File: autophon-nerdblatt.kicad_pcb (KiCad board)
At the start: 2 copper layers, 265 x 140 mm, 18 parts, among them J1 board-edge-connector, U1 74HC74, U2 L298HN, U3 L298HN, U4 L298HN, U5 74AHC04, U6 74HC74, U7 74HC74

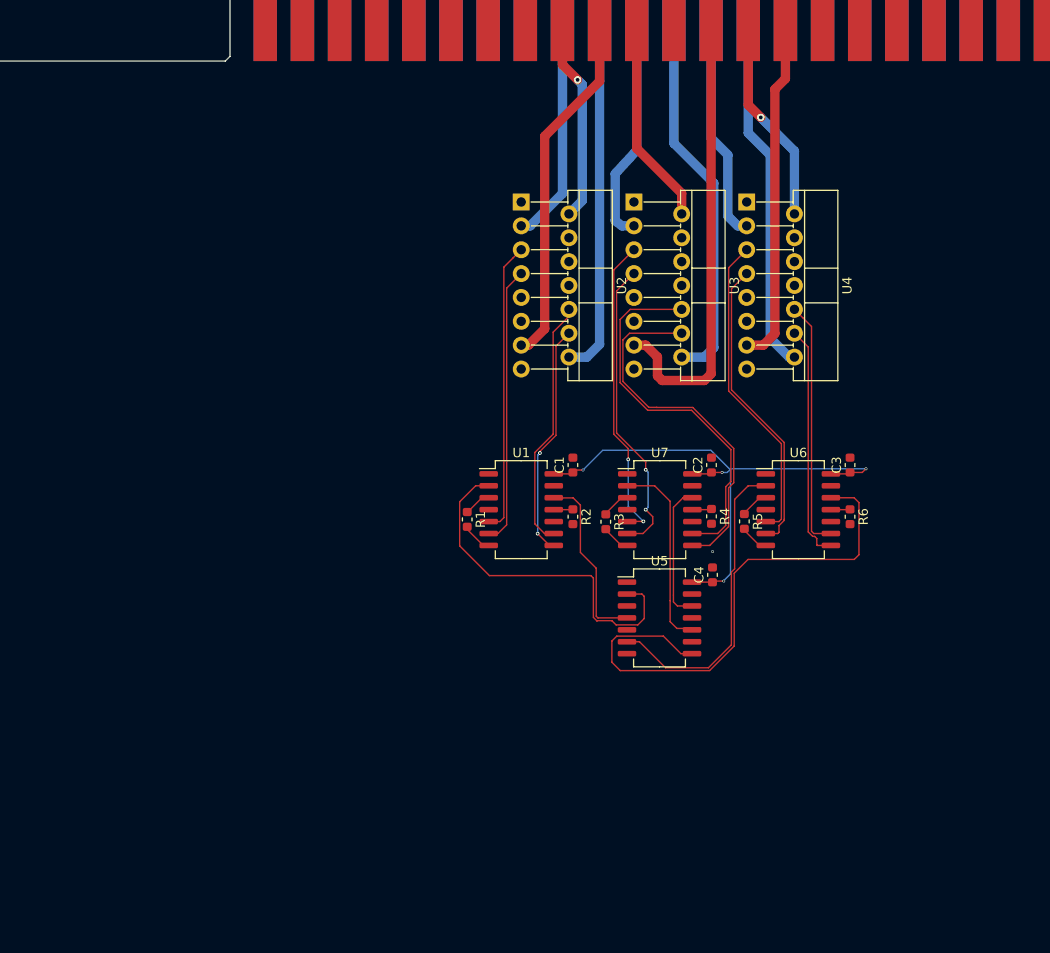
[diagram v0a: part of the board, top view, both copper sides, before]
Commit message: Added footprints.
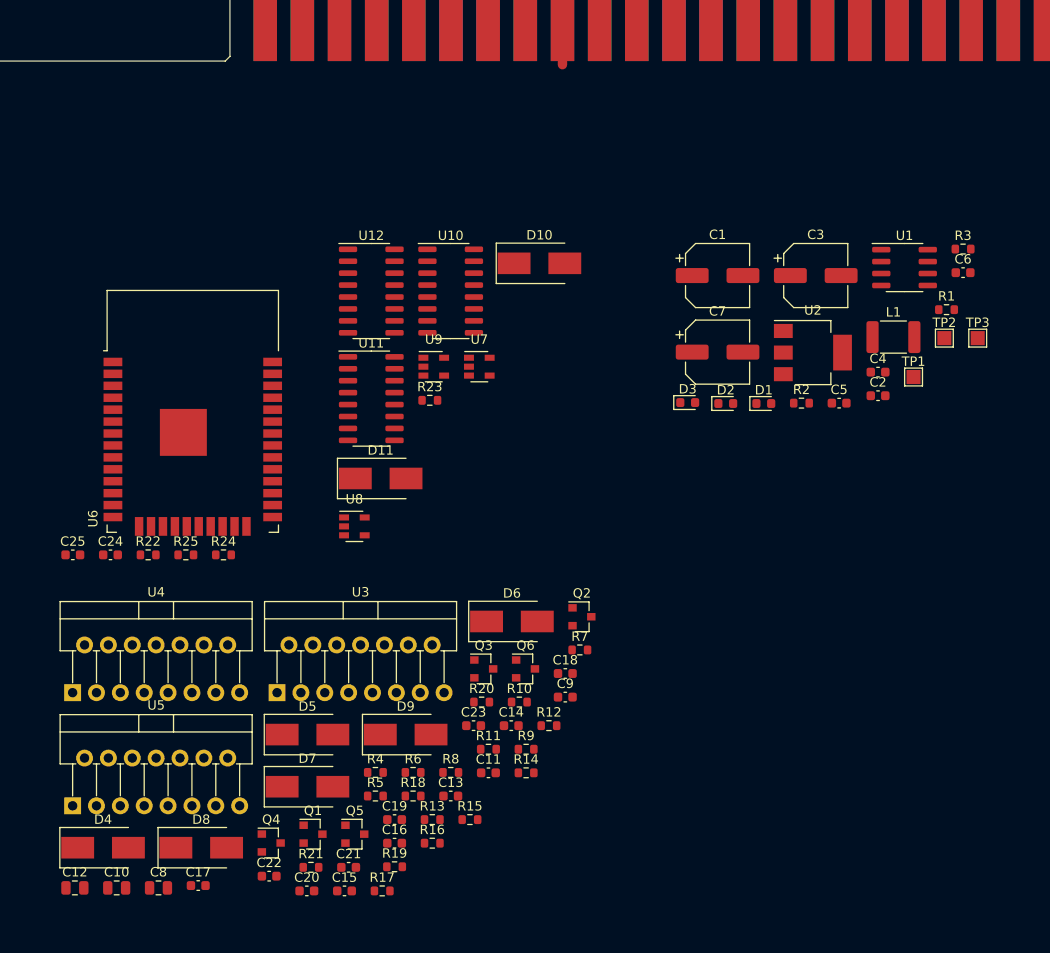
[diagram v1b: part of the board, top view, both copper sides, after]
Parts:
- added C10: 10u, Capacitor_SMD:C_0805_2012Metric, F.Cu at (215.4, 165.5)
- added C11: 100n, Capacitor_SMD:C_0603_1608Metric, F.Cu at (255.0, 153.3)
- added C12: 10u, Capacitor_SMD:C_0805_2012Metric, F.Cu at (211.0, 165.5)
- added C13: 100n, Capacitor_SMD:C_0603_1608Metric, F.Cu at (251.0, 155.7)
- added C14: 100n, Capacitor_SMD:C_0603_1608Metric, F.Cu at (257.4, 148.2)
- added C15: 100n, Capacitor_SMD:C_0603_1608Metric, F.Cu at (239.7, 165.8)
- added C16: 100n, Capacitor_SMD:C_0603_1608Metric, F.Cu at (245.0, 160.8)
- added C17: 100n, Capacitor_SMD:C_0603_1608Metric, F.Cu at (224.1, 165.3)
- added C18: 100n, Capacitor_SMD:C_0603_1608Metric, F.Cu at (263.2, 142.7)
- added C19: 100n, Capacitor_SMD:C_0603_1608Metric, F.Cu at (245.0, 158.2)
- added C20: 100n, Capacitor_SMD:C_0603_1608Metric, F.Cu at (235.7, 165.8)
- added C21: 100n, Capacitor_SMD:C_0603_1608Metric, F.Cu at (240.1, 163.3)
- added C22: 100n, Capacitor_SMD:C_0603_1608Metric, F.Cu at (231.7, 164.3)
- added C23: 100n, Capacitor_SMD:C_0603_1608Metric, F.Cu at (253.4, 148.2)
- added C24: C, Capacitor_SMD:C_0603_1608Metric, F.Cu at (214.8, 130.1)
- added C25: C, Capacitor_SMD:C_0603_1608Metric, F.Cu at (210.8, 130.1)
- added C5: 100n, Capacitor_SMD:C_0603_1608Metric, F.Cu at (292.3, 113.9)
- added C6: 100n, Capacitor_SMD:C_0603_1608Metric, F.Cu at (305.5, 100.0)
- added C7: 22u, Capacitor_SMD:CP_Elec_6.3x7.7, F.Cu at (279.4, 108.5)
- added C8: 10u, Capacitor_SMD:C_0805_2012Metric, F.Cu at (219.9, 165.5)
- added C9: 100n, Capacitor_SMD:C_0603_1608Metric, F.Cu at (263.2, 145.2)
- added D1: LED, LED_SMD:LED_0603_1608Metric, F.Cu at (284.3, 114.0)
- added D10: 5v1, Diode_SMD:D_SMB_Handsoldering, F.Cu at (260.4, 99.0)
- added D11: 5v1, Diode_SMD:D_SMB_Handsoldering, F.Cu at (243.5, 121.9)
- added D2: LED, LED_SMD:LED_0603_1608Metric, F.Cu at (280.3, 114.0)
- added D3: LED, LED_SMD:LED_0603_1608Metric, F.Cu at (276.2, 113.8)
- added D4: 5v1, Diode_SMD:D_SMB_Handsoldering, F.Cu at (214.0, 161.2)
- added D5: 5v1, Diode_SMD:D_SMB_Handsoldering, F.Cu at (235.8, 149.2)
- added D6: 5v1, Diode_SMD:D_SMB_Handsoldering, F.Cu at (257.5, 137.2)
- added D7: 5v1, Diode_SMD:D_SMB_Handsoldering, F.Cu at (235.8, 154.7)
- added D8: 5v1, Diode_SMD:D_SMB_Handsoldering, F.Cu at (224.4, 161.2)
- added D9: 5v1, Diode_SMD:D_SMB_Handsoldering, F.Cu at (246.2, 149.2)
- added L1: 100u, Inductor_SMD:L_1812_4532Metric_Pad1.30x3.40mm_HandSolder, F.Cu at (298.1, 106.9)
- added Q1: BSS84, Package_TO_SOT_SMD:SOT-23, F.Cu at (236.3, 159.8)
- added Q2: BSS84, Package_TO_SOT_SMD:SOT-23, F.Cu at (265.0, 136.7)
- added Q3: BSS84, Package_TO_SOT_SMD:SOT-23, F.Cu at (254.5, 142.2)
- added Q4: BSS84, Package_TO_SOT_SMD:SOT-23, F.Cu at (231.9, 160.7)
- added Q5: BSS84, Package_TO_SOT_SMD:SOT-23, F.Cu at (240.8, 159.8)
- added Q6: BSS84, Package_TO_SOT_SMD:SOT-23, F.Cu at (259.0, 142.2)
- added R10: 10k, Resistor_SMD:R_0603_1608Metric, F.Cu at (258.3, 145.7)
- added R11: 10k, Resistor_SMD:R_0603_1608Metric, F.Cu at (255.0, 150.8)
- added R12: 10k, Resistor_SMD:R_0603_1608Metric, F.Cu at (261.4, 148.2)
- added R13: 10k, Resistor_SMD:R_0603_1608Metric, F.Cu at (249.0, 158.2)
- added R14: 10k, Resistor_SMD:R_0603_1608Metric, F.Cu at (259.0, 153.3)
- added R15: 10k, Resistor_SMD:R_0603_1608Metric, F.Cu at (253.0, 158.2)
- added R16: 51R, Resistor_SMD:R_0603_1608Metric, F.Cu at (249.0, 160.8)
- added R17: 51R, Resistor_SMD:R_0603_1608Metric, F.Cu at (243.7, 165.8)
- added R18: 51R, Resistor_SMD:R_0603_1608Metric, F.Cu at (247.0, 155.7)
- added R19: 51R, Resistor_SMD:R_0603_1608Metric, F.Cu at (245.0, 163.3)
- added R20: 51R, Resistor_SMD:R_0603_1608Metric, F.Cu at (254.3, 145.7)
- added R21: 51R, Resistor_SMD:R_0603_1608Metric, F.Cu at (236.1, 163.3)
- added R22: R, Resistor_SMD:R_0603_1608Metric, F.Cu at (218.8, 130.1)
- added R23: R, Resistor_SMD:R_0603_1608Metric, F.Cu at (248.8, 113.6)
- added R24: R, Resistor_SMD:R_0603_1608Metric, F.Cu at (226.8, 130.1)
- added R25: 10k, Resistor_SMD:R_0603_1608Metric, F.Cu at (222.8, 130.1)
- added R7: 10k, Resistor_SMD:R_0603_1608Metric, F.Cu at (264.7, 140.2)
- added R8: 10k, Resistor_SMD:R_0603_1608Metric, F.Cu at (251.0, 153.2)
- added R9: 10k, Resistor_SMD:R_0603_1608Metric, F.Cu at (259.0, 150.8)
- added TP1: 24V, TestPoint:TestPoint_Pad_1.5x1.5mm, F.Cu at (300.3, 111.1)
- added TP2: 5V, TestPoint:TestPoint_Pad_1.5x1.5mm, F.Cu at (303.5, 107.0)
- added TP3: VCC, TestPoint:TestPoint_Pad_1.5x1.5mm, F.Cu at (307.1, 107.0)
- added U10: 74AHCT595, Package_SO:SOIC-16_3.9x9.9mm_P1.27mm, F.Cu at (251.0, 102.0)
- added U11: 74AHCT595, Package_SO:SOIC-16_3.9x9.9mm_P1.27mm, F.Cu at (242.5, 113.4)
- added U12: 74AHCT595, Package_SO:SOIC-16_3.9x9.9mm_P1.27mm, F.Cu at (242.5, 102.0)
- added U8: SN74LV1T34, Package_TO_SOT_SMD:SOT-23-5, F.Cu at (240.7, 127.0)
- added U9: SN74LV1T34, Package_TO_SOT_SMD:SOT-23-5, F.Cu at (249.2, 110.0)
- C1: value C -> 120u; footprint Capacitor_SMD:C_0603_1608Metric -> Capacitor_SMD:CP_Elec_6.3x7.7
- C2, C4: value C -> 100n
- C3: value C -> 39u; footprint Capacitor_SMD:C_0603_1608Metric -> Capacitor_SMD:CP_Elec_6.3x7.7
- R1, R2, R3, R4, R5, R6: value R -> 10k
- U1: value 74HC74 -> LM2594M-5.0; footprint Package_SO:SO-14_5.3x10.2mm_P1.27mm -> Package_SO:SOIC-8_3.9x4.9mm_P1.27mm
- U2: value L298HN -> AZ1117-3.3; footprint Package_TO_SOT_THT:TO-220F-15_P2.54x5.08mm_StaggerOdd_Lead5.08mm_Vertical -> Package_TO_SOT_SMD:SOT-223-3_TabPin2
- U3, U4: footprint Package_TO_SOT_THT:TO-220F-15_P2.54x5.08mm_StaggerOdd_Lead5.08mm_Vertical -> Package_TO_SOT_THT:TO-220-15_P2.54x2.54mm_StaggerOdd_Lead4.58mm_Vertical
- U5: value 74AHC04 -> L298HN; footprint Package_SO:SO-14_5.3x10.2mm_P1.27mm -> Package_TO_SOT_THT:TO-220-15_P2.54x2.54mm_StaggerOdd_Lead4.58mm_Vertical
- U6: value 74HC74 -> ESP32-WROOM-32; footprint Package_SO:SO-14_5.3x10.2mm_P1.27mm -> RF_Module:ESP32-WROOM-32
- U7: value 74HC74 -> SN74LV1T34; footprint Package_SO:SO-14_5.3x10.2mm_P1.27mm -> Package_TO_SOT_SMD:SOT-23-5
- moved U4 88.7 mm to (210.8, 144.7), turned to 0 degrees
- moved U5 65.6 mm to (210.8, 156.8)
- moved U6 64.9 mm to (223.5, 117.8)
- moved U3 64.6 mm to (232.5, 144.7), turned to 0 degrees
- moved R1 55.7 mm to (303.8, 104.0), turned to 0 degrees
- moved R6 53.9 mm to (247.0, 153.2), turned to 0 degrees
- moved R5 49.0 mm to (243.0, 155.7), turned to 0 degrees
- moved U1 48.3 mm to (299.3, 99.5)
- moved R3 47.8 mm to (305.5, 97.5), turned to 0 degrees
- moved R4 45.0 mm to (243.0, 153.2), turned to 0 degrees
- moved U2 34.9 mm to (289.6, 108.5), turned to 0 degrees
- moved C4 27.9 mm to (296.5, 110.6), turned to 0 degrees
- moved R2 27.2 mm to (288.3, 113.9), turned to 0 degrees
- moved C1 25.4 mm to (279.4, 100.3), turned to 0 degrees
- moved U7 24.5 mm to (254.0, 110.0)
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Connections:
- net ABCDEF.5 renamed ABCDEF_HALL_GND
- net Net-(U5-Pad13) renamed F_MOT_POS
- net Net-(U5-Pad5) renamed E_MOT_POS_DRV
- C1 pad 1: +5V -> +24V
- C2 pad 1: +5V -> +24V
- J1 pad 10B: E.2 -> E_MOT_NEG
- J1 pad 11B: D.2 -> D_MOT_NEG
- J1 pad 12B: C.2 -> C_MOT_NEG
- J1 pad 13B: B.2 -> B_MOT_NEG
- J1 pad 14B: A.2 -> A_MOT_NEG
- J1 pad 19B: ABCDEF.6 -> ABCDEF_HALL_ROTOR
- J1 pad 20B: ABCDEF.4 -> ABCDEF_HALL_INDEX
- J1 pad 23A: A.3 -> A_HALL_PWR
- J1 pad 24A: B.3 -> B_HALL_PWR
- J1 pad 25A: C.3 -> C_HALL_PWR
- J1 pad 27A: D.3 -> D_HALL_PWR
- J1 pad 28A: E.3 -> E_HALL_PWR
- J1 pad 29A: F.3 -> F_HALL_PWR
- J1 pad 31A: A.1 -> A_MOT_POS
- J1 pad 32A: B.1 -> B_MOT_POS
- J1 pad 33A: C.1 -> C_MOT_POS
- J1 pad 35A: D.1 -> D_MOT_POS
- J1 pad 36A: E.1 -> E_MOT_POS
- J1 pad 37A: F.1 -> F_MO_POS
- J1 pad 9B: F.2 -> F_MOT_NEG
- R1 pad 1: Net-(R1-Pad1) -> +24V
- R1 pad 2: GND -> Net-(D1-Pad2)
- R2 pad 1: Net-(R2-Pad1) -> +5V
- R2 pad 2: GND -> Net-(D2-Pad2)
- R3 pad 1: Net-(R3-Pad1) -> VCC
- R3 pad 2: GND -> Net-(D3-Pad2)
- R4 pad 1: Net-(R4-Pad1) -> +5V
- R4 pad 2: GND -> ~A_HALL_PWR_EN~
- R5 pad 1: Net-(R5-Pad1) -> +5V
- R5 pad 2: GND -> ~B_HALL_PWR_EN~
- R6 pad 1: Net-(R6-Pad1) -> +5V
- R6 pad 2: GND -> ~C_HALL_PWR_EN~
- U1 pad 3: Net-(R1-Pad1) -> Net-(U1-Pad3)
- U1 pad 4: Net-(U1-Pad4) -> +5V
- U1 pad 5: A_IN1 -> Net-(U1-Pad5)
- U1 pad 6: A_IN2 -> GND
- U1 pad 7: GND -> +24V
- U1 pad 8: B_IN4 -> Net-(L1-Pad1)
- U2 pad 2: A.1 -> VCC
- U2 pad 3: A.2 -> +5V
- U3 pad 1: Net-(U3-Pad1) -> GND
- U3 pad 10: D_IN3 -> B_MOT_POS_DRV
- U3 pad 11: D_EN -> GLOBAL_MOT_EN
- U3 pad 12: D_IN4 -> B_MOT_NEG_DRV
- U3 pad 13: D.1 -> B_MOT_POS
- U3 pad 14: D.2 -> B_MOT_NEG
- U3 pad 15: Net-(U3-Pad15) -> GND
- U3 pad 2: C.1 -> A_MOT_POS
- U3 pad 3: C.2 -> A_MOT_NEG
- U3 pad 4: Net-(U3-Pad4) -> +5V
- U3 pad 5: C_IN1 -> A_MOT_POS_DRV
- U3 pad 6: C_EN -> GLOBAL_MOT_EN
- U3 pad 7: C_IN2 -> A_MOT_NEG_DRV
- U3 pad 9: Net-(U3-Pad9) -> +24V
- U4 pad 1: Net-(U4-Pad1) -> GND
- U4 pad 10: F_IN3 -> D_MOT_POS_DRV
- U4 pad 11: F_EN -> GLOBAL_MOT_EN
- U4 pad 12: F_IN4 -> D_MOT_NEG_DRV
- U4 pad 13: F.1 -> D_MOT_POS
- U4 pad 14: F.2 -> D_MOT_NEG
- U4 pad 15: Net-(U4-Pad15) -> GND
- U4 pad 2: E.1 -> C_MOT_POS
- U4 pad 3: E.2 -> C_MOT_NEG
- U4 pad 4: Net-(U4-Pad4) -> +5V
- U4 pad 5: E_IN1 -> C_MOT_POS_DRV
- U4 pad 6: E_EN -> GLOBAL_MOT_EN
- U4 pad 7: E_IN2 -> C_MOT_NEG_DRV
- U4 pad 9: Net-(U4-Pad9) -> +24V
- U5 pad 1: Net-(U5-Pad1) -> GND
- U5 pad 10: Net-(U5-Pad10) -> F_MOT_POS_DRV
- U5 pad 11: Net-(U5-Pad11) -> GLOBAL_MOT_EN
- U5 pad 12: Net-(U5-Pad12) -> F_MOT_NEG_DRV
- U5 pad 14: +5V -> F_MOT_NEG
- U5 pad 2: Net-(U1-Pad2) -> E_MOT_POS
- U5 pad 3: Net-(U5-Pad3) -> E_MOT_NEG
- U5 pad 4: Net-(U1-Pad12) -> +5V
- U5 pad 6: Net-(U5-Pad6) -> GLOBAL_MOT_EN
- U5 pad 7: GND -> E_MOT_NEG_DRV
- U5 pad 8: Net-(U5-Pad8) -> GND
- U5 pad 9: Net-(U5-Pad9) -> +24V
- U6 pad 10: Net-(U6-Pad10) -> /ESP32_Shiftregs/~HALL_EN_3V~
- U6 pad 11: Net-(R6-Pad1) -> /ESP32_Shiftregs/MOT_EN_3V
- U6 pad 12: Net-(U5-Pad8) -> /ESP32_Shiftregs/HALL_ROTOR_3V
- U6 pad 14: +5V -> Net-(U6-Pad14)
- U6 pad 2: Net-(U5-Pad6) -> Net-(U6-Pad2)
- U6 pad 3: Net-(R5-Pad1) -> Net-(U6-Pad3)
- U6 pad 5: E_IN1 -> Net-(U6-Pad5)
- U6 pad 6: E_IN2 -> /ESP32_Shiftregs/SPI_SCLK
- U6 pad 7: GND -> /ESP32_Shiftregs/~SPI_CS0~
- U6 pad 8: F_IN4 -> /ESP32_Shiftregs/HALL_INDEX_3V
- U6 pad 9: F_IN3 -> /ESP32_Shiftregs/SPI_COPI
- U7 pad 1: Net-(U7-Pad1) -> (no net)
- U7 pad 2: Net-(U5-Pad10) -> ABCDEF_HALL_ROTOR
- U7 pad 3: Net-(R3-Pad1) -> GND
- U7 pad 4: Net-(U7-Pad4) -> /ESP32_Shiftregs/HALL_ROTOR_3V
- U7 pad 5: C_IN1 -> VCC
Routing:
- net +5V: track 59.0 -> 0.00 mm, vias 4 -> 0
- net Net-(U5-Pad8): track 57.8 -> 0.00 mm
- net D.1: track 44.5 -> 0.00 mm
- net D_IN3: track 40.7 -> 0.00 mm
- net D_IN4: track 39.0 -> 0.00 mm
- net Net-(U1-Pad2): track 38.6 -> 0.00 mm
- net D.2: track 36.1 -> 0.00 mm
- net B.1: track 34.1 -> 0.00 mm
- net B.2: track 34.0 -> 0.00 mm
- net F.2: track 33.9 -> 0.00 mm
- net E_IN1: track 33.6 -> 0.00 mm
- net F.1: track 33.0 -> 0.00 mm
- net C_IN1: track 32.8 -> 0.00 mm, vias 2 -> 0
- net Net-(U5-Pad6): track 32.8 -> 0.00 mm
- net C_IN2: track 32.3 -> 0.00 mm, vias 2 -> 0
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
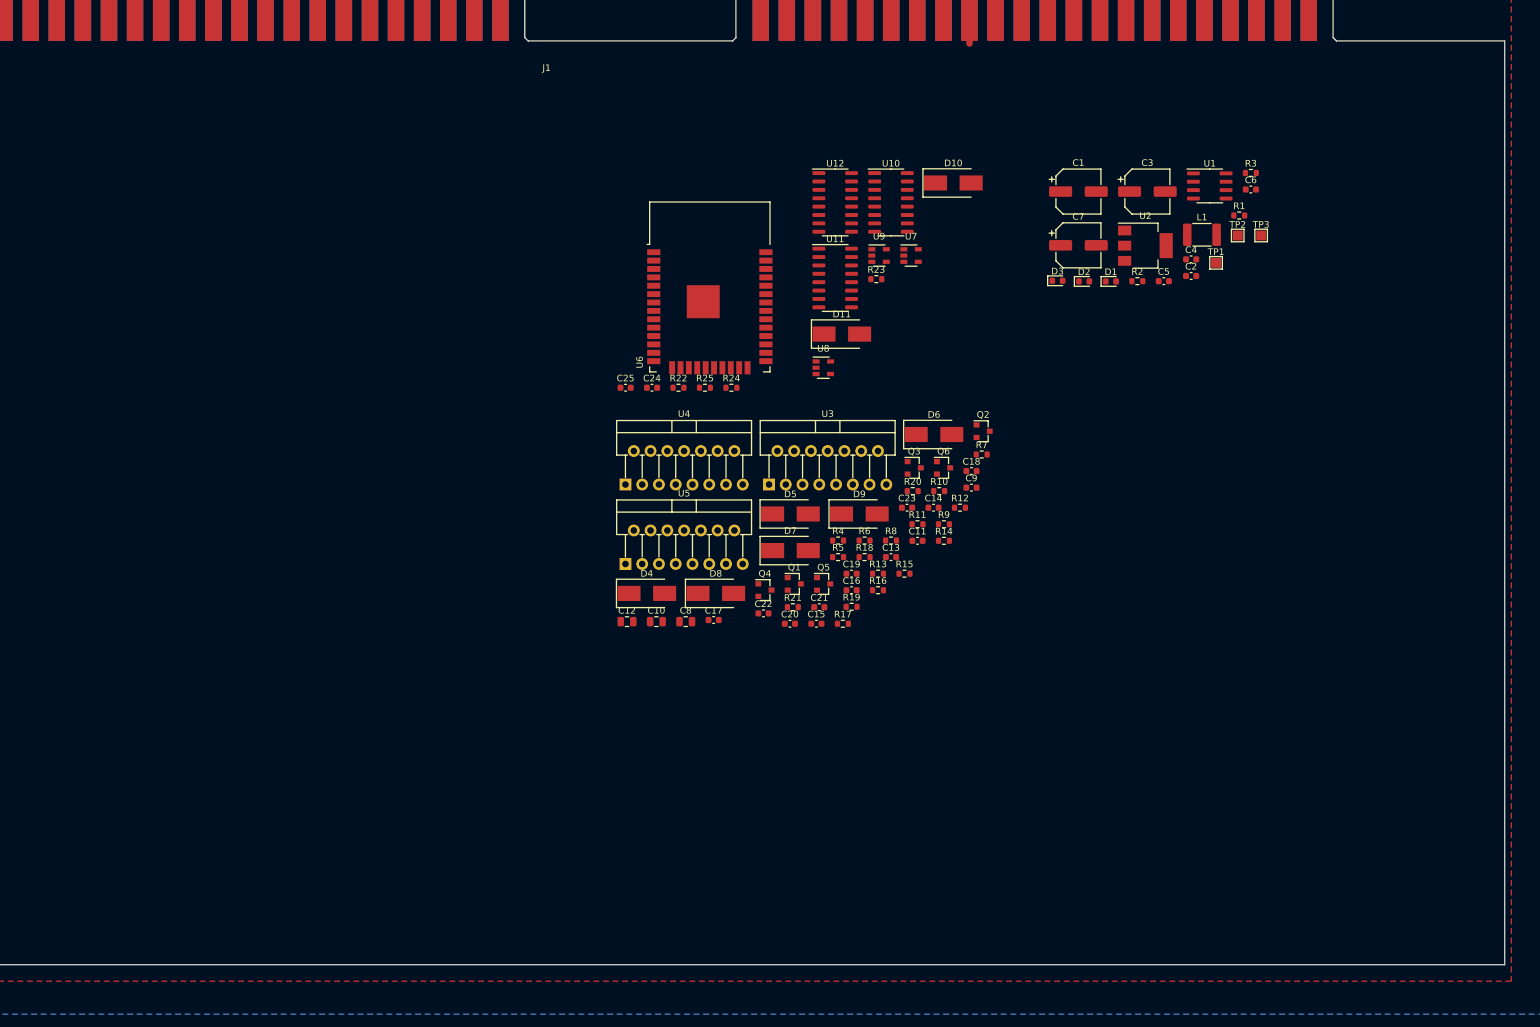
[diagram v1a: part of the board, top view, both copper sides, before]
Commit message: caps for long high impedance traces. distributor info.
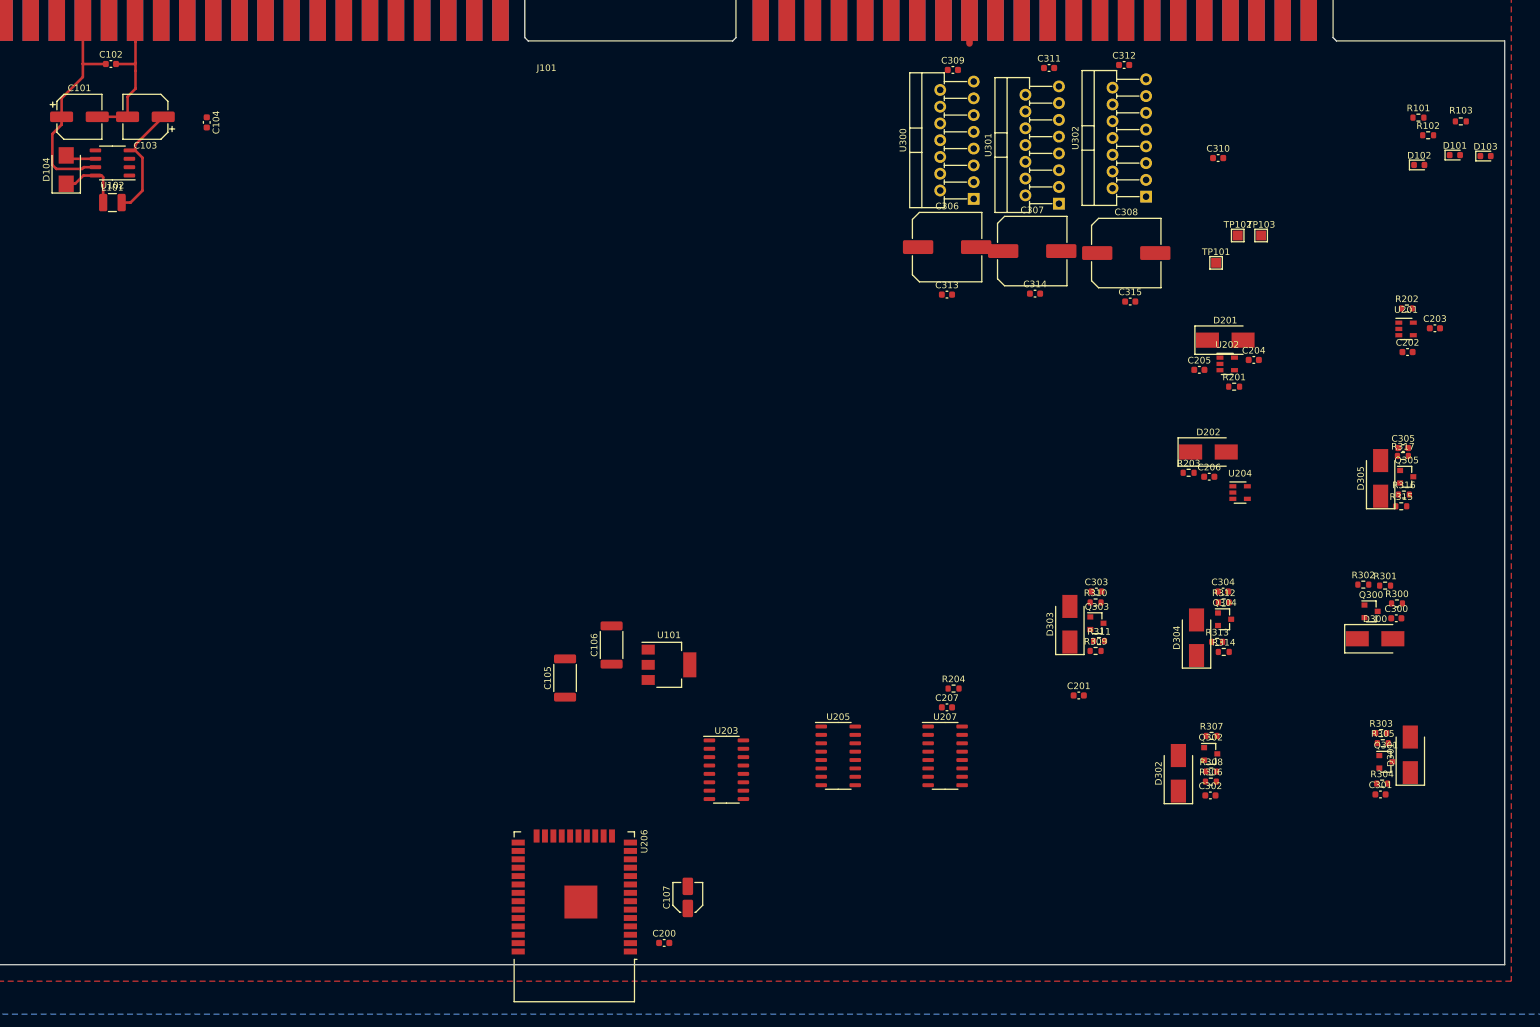
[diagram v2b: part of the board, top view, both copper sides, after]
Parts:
- removed C10, C12, C8: 10u, Capacitor_SMD:C_0805_2012Metric
- removed C5, C6: 100n, Capacitor_SMD:C_0603_1608Metric
- removed U2: AZ1117-3.3, Package_TO_SOT_SMD:SOT-223-3_TabPin2
- added C105: 10u, Capacitor_SMD:C_2512_6332Metric, F.Cu at (201.6, 174.1)
- added C106: 10u, Capacitor_SMD:C_2512_6332Metric, F.Cu at (208.7, 169.1)
- added C200: 100n, Capacitor_SMD:C_0603_1608Metric, F.Cu at (216.6, 214.2)
- added C201: 100n, Capacitor_SMD:C_0603_1608Metric, F.Cu at (279.4, 176.7)
- added C202: 1n, Capacitor_SMD:C_0603_1608Metric, F.Cu at (329.3, 124.7)
- added C204: 1n, Capacitor_SMD:C_0603_1608Metric, F.Cu at (306.0, 125.8)
- added C206: 1n, Capacitor_SMD:C_0603_1608Metric, F.Cu at (299.2, 143.6)
- added C207: 1n, Capacitor_SMD:C_0603_1608Metric, F.Cu at (259.5, 178.5)
- added C306: 470uF, Capacitor_SMD:C_Elec_10x10.2, F.Cu at (259.5, 108.8)
- added C307: 470uF, Capacitor_SMD:C_Elec_10x10.2, F.Cu at (272.4, 109.3)
- added C308: 470uF, Capacitor_SMD:C_Elec_10x10.2, F.Cu at (286.6, 109.7)
- added D104: MBRS130, Diode_SMD:D_SMB, F.Cu at (126.0, 97.0)
- added U101: LM1117-3.3, Package_TO_SOT_SMD:SOT-223-3_TabPin2, F.Cu at (217.3, 172.1)
- C102: renamed from C2; value 100n -> 100n/25V
- C103: renamed from C3; value 39u -> 120u
- C107: renamed from C7; footprint Capacitor_SMD:CP_Elec_6.3x7.7 -> Capacitor_SMD:C_Elec_4x5.8
- C203: renamed from C25; value C -> 1n
- C205: renamed from C24; value C -> 1n
- C313: renamed from C9; value 100n -> 100n/25V
- C314: renamed from C11; value 100n -> 100n/25V
- C315: renamed from C13; value 100n -> 100n/25V
- D101: renamed from D1; value LED -> LED gn
- D102: renamed from D2; value LED -> LED gn
- D103: renamed from D3; value LED -> LED gn
- L101: renamed from L1; value 100u -> 100uH; footprint Inductor_SMD:L_1812_4532Metric_Pad1.30x3.40mm_HandSolder -> Inductor_SMD:L_1210_3225Metric
- R101: renamed from R1; value 10k -> 1k2
- R102: renamed from R2; value 10k -> 200R
- R103: renamed from R3; value 10k -> 100R
- R201: renamed from R23; value R -> 4k7
- R203: renamed from R22; value R -> 4k7
- R204: renamed from R24; value R -> 10k
- U102: renamed from U1; footprint Package_SO:SOIC-8_3.9x4.9mm_P1.27mm -> Package_SO:SO-8_3.9x4.9mm_P1.27mm
- U203: renamed from U10; footprint Package_SO:SOIC-16_3.9x9.9mm_P1.27mm -> Package_SO:SO-16_3.9x9.9mm_P1.27mm
- U205: renamed from U11; footprint Package_SO:SOIC-16_3.9x9.9mm_P1.27mm -> Package_SO:SO-16_3.9x9.9mm_P1.27mm
- U207: renamed from U12; footprint Package_SO:SOIC-16_3.9x9.9mm_P1.27mm -> Package_SO:SO-16_3.9x9.9mm_P1.27mm
- moved C102 166.8 mm to (132.8, 81.0)
- moved U102 166.3 mm to (133.0, 96.0), turned to 180 degrees
- moved L101 165.2 mm to (133.0, 102.0)
- moved C103 152.3 mm to (138.0, 89.0), turned to 180 degrees
- moved C101 151.8 mm to (128.0, 89.0)
- moved C104 150.6 mm to (147.3, 89.8), turned to -90 degrees
- moved C203 123.0 mm to (333.4, 121.0)
- moved C107 115.2 mm to (220.2, 207.3), turned to 90 degrees
- moved D300 110.6 mm to (324.4, 168.1)
- moved R202 107.1 mm to (329.2, 118.0)
- moved C312 104.6 mm to (286.3, 81.2)
- moved D301 100.8 mm to (329.7, 185.7), turned to 90 degrees
- moved U302 96.6 mm to (289.6, 101.1), turned to 90 degrees
- moved R315 93.5 mm to (328.3, 148.0)
- moved C310 93.2 mm to (300.6, 95.2)
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- renumbered C1 to C101, C4 to C104, C18 to C300, C19 to C301, C20 to C302, C21 to C303, C22 to C304, C23 to C305, C14 to C309, C15 to C310, C16 to C311, C17 to C312, D11 to D201, D10 to D202, D4 to D300, D5 to D301, D6 to D302, D7 to D303, D8 to D304, D9 to D305, J1 to J101, Q1 to Q300, Q2 to Q301, Q3 to Q302, Q4 to Q303, Q5 to Q304, Q6 to Q305, R25 to R202, R16 to R300, R4 to R301, R10 to R302, R17 to R303, R5 to R304, R11 to R305, R18 to R306, R6 to R307, R12 to R308, R19 to R309, R7 to R310, R13 to R311, R20 to R312, R8 to R313, R14 to R314, R21 to R315, R9 to R316, R15 to R317, TP1 to TP101, TP2 to TP102, TP3 to TP103, U9 to U201, U8 to U202, U7 to U204, U6 to U206, U3 to U300, U4 to U301, U5 to U302
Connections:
- net Net-(J1-Pad12A) renamed no_connect_126
- net Net-(J1-Pad13A) renamed no_connect_127
- net Net-(J1-Pad14A) renamed no_connect_128
- net Net-(J1-Pad15A) renamed no_connect_129
- net Net-(J1-Pad15B) renamed no_connect_130
- net Net-(J1-Pad16A) renamed no_connect_131
- net Net-(J1-Pad16B) renamed no_connect_132
- net Net-(J1-Pad17A) renamed no_connect_133
- net Net-(J1-Pad18A) renamed no_connect_134
- net Net-(J1-Pad19A) renamed no_connect_135
- net Net-(J1-Pad1A) renamed no_connect_136
- net Net-(J1-Pad1B) renamed no_connect_137
- net Net-(J1-Pad20A) renamed no_connect_138
- net Net-(J1-Pad21A) renamed no_connect_139
- net Net-(J1-Pad21B) renamed no_connect_140
- net Net-(J1-Pad22A) renamed no_connect_141
- net Net-(J1-Pad22B) renamed no_connect_142
- net Net-(J1-Pad23B) renamed no_connect_143
- net Net-(J1-Pad24B) renamed no_connect_144
- net Net-(J1-Pad25B) renamed no_connect_145
- net Net-(J1-Pad26A) renamed no_connect_146
- net Net-(J1-Pad26B) renamed no_connect_147
- net Net-(J1-Pad27B) renamed no_connect_148
- net Net-(J1-Pad28B) renamed no_connect_149
- net Net-(J1-Pad29B) renamed no_connect_150
- net Net-(J1-Pad2A) renamed no_connect_151
- net Net-(J1-Pad2B) renamed no_connect_152
- net Net-(J1-Pad30A) renamed no_connect_153
- net Net-(J1-Pad30B) renamed no_connect_154
- net Net-(J1-Pad31B) renamed no_connect_155
- net Net-(J1-Pad32B) renamed no_connect_156
- net Net-(J1-Pad33B) renamed no_connect_157
- net Net-(J1-Pad34A) renamed no_connect_158
- net Net-(J1-Pad36B) renamed no_connect_159
- net Net-(J1-Pad38A) renamed no_connect_160
- net Net-(J1-Pad38B) renamed no_connect_161
- net Net-(J1-Pad39A) renamed no_connect_162
- net Net-(J1-Pad3A) renamed no_connect_163
- net Net-(J1-Pad3B) renamed no_connect_164
- net Net-(J1-Pad40A) renamed no_connect_165
- net Net-(J1-Pad40B) renamed no_connect_166
- net Net-(J1-Pad41A) renamed no_connect_167
- net Net-(J1-Pad41B) renamed no_connect_168
- net Net-(J1-Pad42A) renamed no_connect_169
- net Net-(J1-Pad42B) renamed no_connect_170
- net Net-(J1-Pad43A) renamed no_connect_171
- net Net-(J1-Pad43B) renamed no_connect_172
- net Net-(J1-Pad44A) renamed no_connect_173
- net Net-(J1-Pad44B) renamed no_connect_174
- net Net-(J1-Pad4A) renamed no_connect_175
- net Net-(J1-Pad4B) renamed no_connect_176
- net Net-(J1-Pad5A) renamed no_connect_177
- net Net-(J1-Pad5B) renamed no_connect_178
- net Net-(J1-Pad6B) renamed no_connect_179
- net Net-(J1-Pad7A) renamed no_connect_180
- net Net-(J1-Pad7B) renamed no_connect_181
- net Net-(J1-Pad8B) renamed no_connect_182
- net Net-(J1-Pad9A) renamed no_connect_183
- net Net-(U6-Pad32) renamed no_connect_184
- J101 pad 37B: Net-(J1-Pad37B) -> GND
- J101 pad 39B: Net-(J1-Pad39B) -> +24V
- J101 pad 6A: Net-(J1-Pad39B) -> +24V
- J101 pad 8A: Net-(J1-Pad37B) -> GND
- U102 pad 1: Net-(U1-Pad1) -> GND
- U102 pad 2: Net-(U1-Pad2) -> GND
- U102 pad 3: Net-(U1-Pad3) -> GND
- U206 pad 2: Net-(U6-Pad2) -> VCC
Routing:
- net +24V: track 0.00 -> 31.1 mm
- net GND: track 0.00 -> 24.3 mm
- net +5V: track 0.00 -> 18.2 mm
- net Net-(D104-Pad1): track 0.00 -> 10.1 mm
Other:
- net class Default removed
- net class Motor removed
